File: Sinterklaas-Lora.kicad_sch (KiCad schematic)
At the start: 1 part, among them U1 Pico

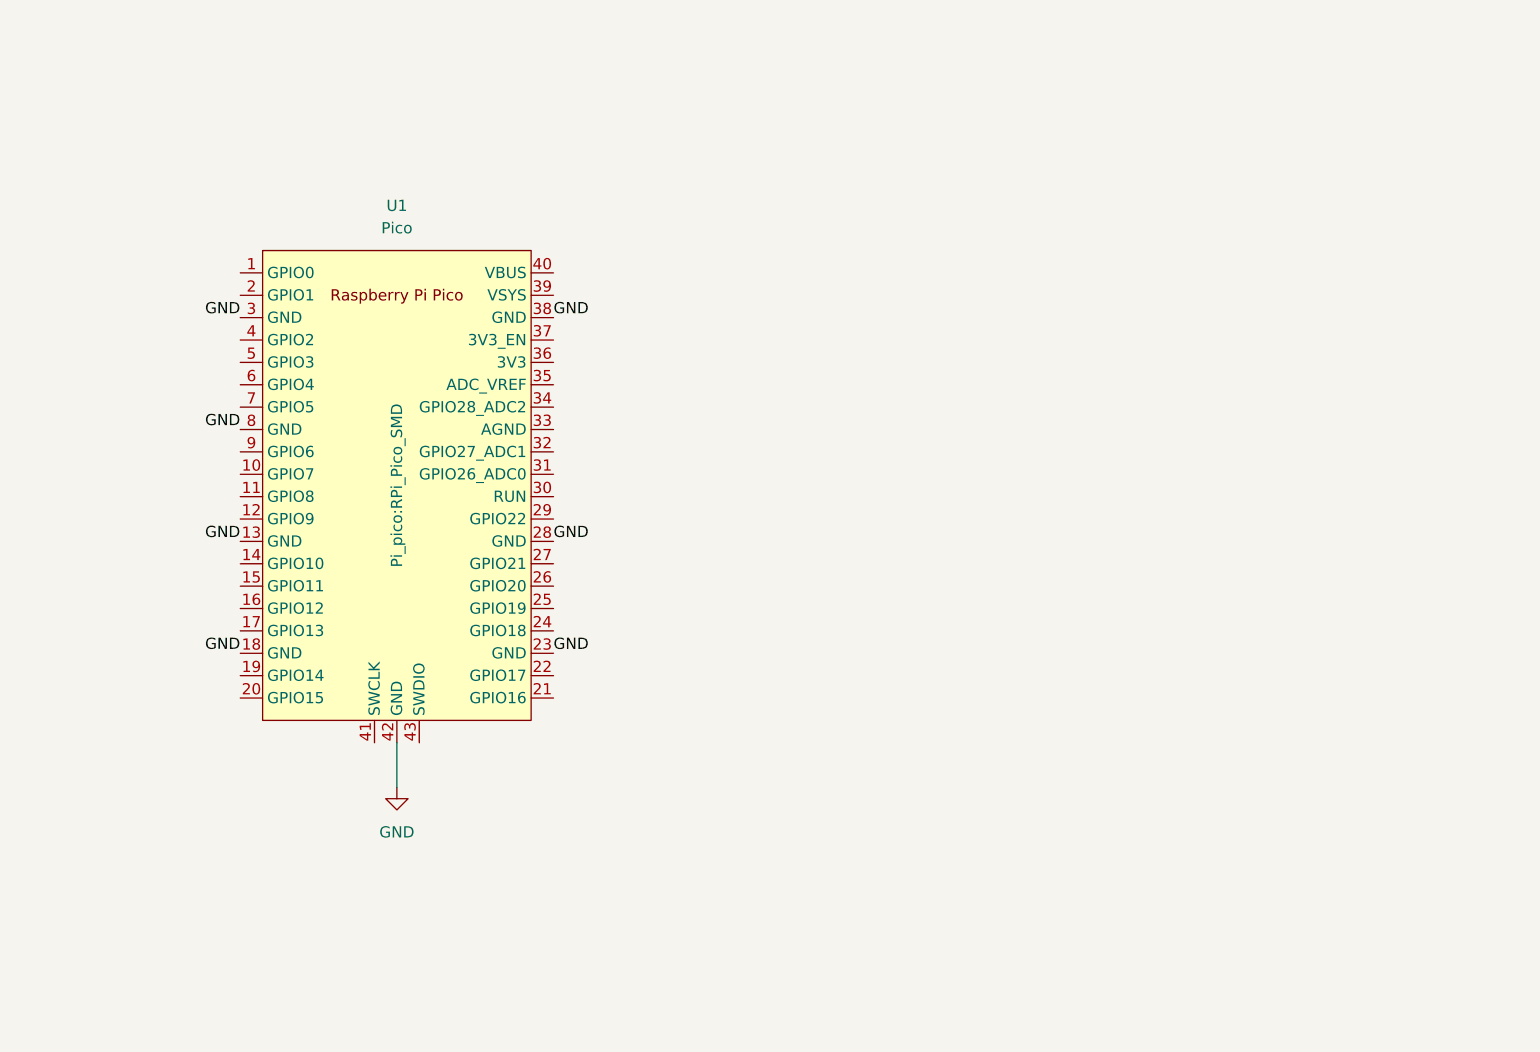
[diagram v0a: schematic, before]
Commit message: Added battery holder
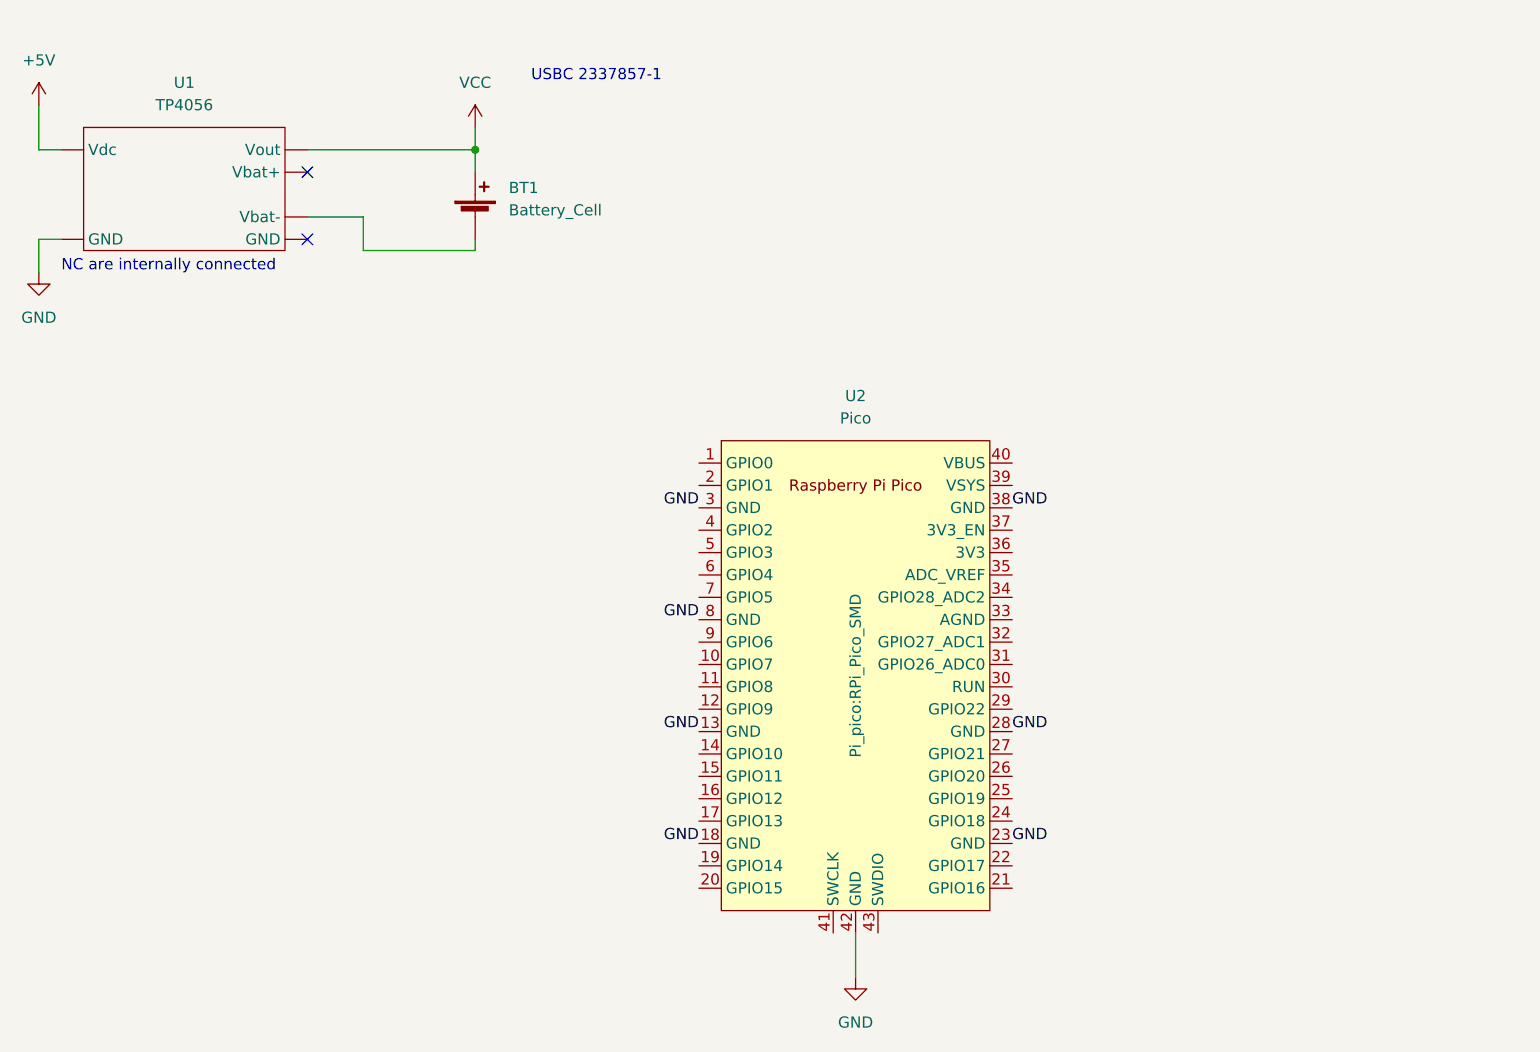
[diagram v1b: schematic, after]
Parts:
- added BT1: Battery_Cell, Pi_pico:1042P, symbol Device:Battery_Cell
- added U1: TP4056, Pi_pico:TP4056-Module, symbol _projectsymbol:TP4056
- renumbered U1 to U2
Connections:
- net GND: now also U1.2 (GND)
- new net: BT1.2 (-), U1.6 (Vbat-)
- new net +5V: U1.1 (Vdc)
- new net VCC: BT1.1 (+), U1.3 (Vout)
- no-connect marks 0 -> 2
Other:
- note added: "NC are internally connected"
- note added: "USBC 2337857-1"
- moved on the sheet: U2
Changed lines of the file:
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@@
 (kicad_sch (version 20211123) (generator eeschema)
   (paper "A3")
-  (wire (pts (xy 83.82 96.52) (xy 83.82 101.6))
-    (stroke (width 0) (type default) (color 0 0 0 0))
-  )
-  (label "GND" (at 101.6 86.36 0)
-    (effects (font (size 1.27 1.27)) (justify left bottom))
-  )
-  (label "GND" (at 66.04 60.96 180)
-    (effects (font (size 1.27 1.27)) (justify right bottom))
-  )
-  (label "GND" (at 101.6 48.26 0)
-    (effects (font (size 1.27 1.27)) (justify left bottom))
-  )
-  (label "GND" (at 66.04 48.26 180)
-    (effects (font (size 1.27 1.27)) (justify right bottom))
-  )
-  (label "GND" (at 101.6 73.66 0)
-    (effects (font (size 1.27 1.27)) (justify left bottom))
-  )
-  (label "GND" (at 66.04 73.66 180)
-    (effects (font (size 1.27 1.27)) (justify right bottom))
-  )
-  (label "GND" (at 66.04 86.36 180)
-    (effects (font (size 1.27 1.27)) (justify right bottom))
-  )
-  (symbol (lib_id "power:GND") (at 83.82 101.6 0) (unit 1)
-    (in_bom yes) (on_board yes) (fields_autoplaced)
-    (property "Reference" "#PWR0101" (id 0) (at 83.82 107.95 0)
-      (effects (font (size 1.27 1.27)) hide)
-    )
-    (property "Value" "GND" (id 1) (at 83.82 106.68 0))
-    (property "Footprint" "" (id 2) (at 83.82 101.6 0)
-      (effects (font (size 1.27 1.27)) hide)
-    )
-    (property "Datasheet" "" (id 3) (at 83.82 101.6 0)
-      (effects (font (size 1.27 1.27)) hide)
-    )
-    (pin "1")
-  )
-  (symbol (lib_id "Pi-Pico:Pico") (at 83.82 67.31 0) (unit 1)
-    (in_bom yes) (on_board yes) (fields_autoplaced)
-    (property "Reference" "U1" (id 0) (at 83.82 35.56 0))
-    (property "Value" "Pico" (id 1) (at 83.82 38.1 0))
-    (property "Footprint" "Pi_pico:RPi_Pico_SMD" (id 2) (at 83.82 67.31 90))
-    (property "Datasheet" "" (id 3) (at 83.82 67.31 0)
+  (junction (at 92.71 29.21) (diameter 0) (color 0 0 0 0)
+  )
+  (no_connect (at 73.66 39.37))
+  (no_connect (at 73.66 31.75))
+  (wire (pts (xy 73.66 36.83) (xy 80.01 36.83))
+    (stroke (width 0) (type default) (color 0 0 0 0))
+  )
+  (wire (pts (xy 92.71 26.67) (xy 92.71 29.21))
+    (stroke (width 0) (type default) (color 0 0 0 0))
+  )
+  (wire (pts (xy 43.18 43.18) (xy 43.18 39.37))
+    (stroke (width 0) (type default) (color 0 0 0 0))
+  )
+  (wire (pts (xy 43.18 29.21) (xy 45.72 29.21))
+    (stroke (width 0) (type default) (color 0 0 0 0))
+  )
+  (wire (pts (xy 73.66 29.21) (xy 92.71 29.21))
+    (stroke (width 0) (type default) (color 0 0 0 0))
+  )
+  (wire (pts (xy 43.18 39.37) (xy 45.72 39.37))
+    (stroke (width 0) (type default) (color 0 0 0 0))
+  )
+  (wire (pts (xy 43.18 24.13) (xy 43.18 29.21))
+    (stroke (width 0) (type default) (color 0 0 0 0))
+  )
+  (wire (pts (xy 92.71 29.21) (xy 92.71 31.75))
+    (stroke (width 0) (type default) (color 0 0 0 0))
+  )
+  (wire (pts (xy 135.89 118.11) (xy 135.89 123.19))
+    (stroke (width 0) (type default) (color 0 0 0 0))
+  )
+  (wire (pts (xy 80.01 40.64) (xy 92.71 40.64))
+    (stroke (width 0) (type default) (color 0 0 0 0))
+  )
+  (wire (pts (xy 80.01 36.83) (xy 80.01 40.64))
+    (stroke (width 0) (type default) (color 0 0 0 0))
+  )
+  (wire (pts (xy 92.71 40.64) (xy 92.71 39.37))
+    (stroke (width 0) (type default) (color 0 0 0 0))
+  )
+  (text "USBC 2337857-1" (at 99.06 21.59 0)
+    (effects (font (size 1.27 1.27)) (justify left bottom))
+  )
+  (text "NC are internally connected" (at 45.72 43.18 0)
+    (effects (font (size 1.27 1.27)) (justify left bottom))
+  )
+  (label "GND" (at 153.67 107.95 0)
+    (effects (font (size 1.27 1.27)) (justify left bottom))
+  )
+  (label "GND" (at 118.11 82.55 180)
+    (effects (font (size 1.27 1.27)) (justify right bottom))
+  )
+  (label "GND" (at 153.67 69.85 0)
+    (effects (font (size 1.27 1.27)) (justify left bottom))
+  )
+  (label "GND" (at 118.11 69.85 180)
+    (effects (font (size 1.27 1.27)) (justify right bottom))
+  )
+  (label "GND" (at 153.67 95.25 0)
+    (effects (font (size 1.27 1.27)) (justify left bottom))
+  )
+  (label "GND" (at 118.11 95.25 180)
+    (effects (font (size 1.27 1.27)) (justify right bottom))
+  )
+  (label "GND" (at 118.11 107.95 180)
+    (effects (font (size 1.27 1.27)) (justify right bottom))
+  )
+  (symbol (lib_id "power:GND") (at 135.89 123.19 0) (unit 1)
+    (in_bom yes) (on_board yes) (fields_autoplaced)
+    (property "Reference" "#PWR03" (id 0) (at 135.89 129.54 0)
+      (effects (font (size 1.27 1.27)) hide)
+    )
+    (property "Value" "GND" (id 1) (at 135.89 128.27 0))
+    (property "Footprint" "" (id 2) (at 135.89 123.19 0)
+      (effects (font (size 1.27 1.27)) hide)
+    )
+    (property "Datasheet" "" (id 3) (at 135.89 123.19 0)
+      (effects (font (size 1.27 1.27)) hide)
+    )
+    (pin "1")
+  )
+  (symbol (lib_id "power:VCC") (at 92.71 26.67 0) (unit 1)
+    (in_bom yes) (on_board yes) (fields_autoplaced)
+    (property "Reference" "#PWR?" (id 0) (at 92.71 30.48 0)
+      (effects (font (size 1.27 1.27)) hide)
+    )
+    (property "Value" "VCC" (id 1) (at 92.71 21.59 0))
+    (property "Footprint" "" (id 2) (at 92.71 26.67 0)
+      (effects (font (size 1.27 1.27)) hide)
+    )
+    (property "Datasheet" "" (id 3) (at 92.71 26.67 0)
+      (effects (font (size 1.27 1.27)) hide)
+    )
+    (pin "1")
+  )
+  (symbol (lib_id "Device:Battery_Cell") (at 92.71 36.83 0) (unit 1)
+    (in_bom yes) (on_board yes) (fields_autoplaced)
+    (property "Reference" "BT1" (id 0) (at 96.52 33.5279 0)
+      (effects (font (size 1.27 1.27)) (justify left))
+    )
+    (property "Value" "Battery_Cell" (id 1) (at 96.52 36.0679 0)
+      (effects (font (size 1.27 1.27)) (justify left))
+    )
+    (property "Footprint" "Pi_pico:1042P" (id 2) (at 92.71 35.306 90)
+      (effects (font (size 1.27 1.27)) hide)
+    )
+    (property "Datasheet" "~" (id 3) (at 92.71 35.306 90)
+      (effects (font (size 1.27 1.27)) hide)
+    )
+    (pin "1")
+    (pin "2")
+  )
+  (symbol (lib_id "Pi-Pico:Pico") (at 135.89 88.9 0) (unit 1)
+    (in_bom yes) (on_board yes) (fields_autoplaced)
+    (property "Reference" "U2" (id 0) (at 135.89 57.15 0))
+    (property "Value" "Pico" (id 1) (at 135.89 59.69 0))
+    (property "Footprint" "Pi_pico:RPi_Pico_SMD" (id 2) (at 135.89 88.9 90))
+    (property "Datasheet" "" (id 3) (at 135.89 88.9 0)
       (effects (font (size 1.27 1.27)) hide)
     )
@@
     (pin "9")
   )
+  (symbol (lib_id "power:GND") (at 43.18 43.18 0) (unit 1)
+    (in_bom yes) (on_board yes) (fields_autoplaced)
+    (property "Reference" "#PWR02" (id 0) (at 43.18 49.53 0)
+      (effects (font (size 1.27 1.27)) hide)
+    )
+    (property "Value" "GND" (id 1) (at 43.18 48.26 0))
+    (property "Footprint" "" (id 2) (at 43.18 43.18 0)
+      (effects (font (size 1.27 1.27)) hide)
+    )
+    (property "Datasheet" "" (id 3) (at 43.18 43.18 0)
+      (effects (font (size 1.27 1.27)) hide)
+    )
+    (pin "1")
+  )
+  (symbol (lib_id "power:+5V") (at 43.18 24.13 0) (unit 1)
+    (in_bom yes) (on_board yes) (fields_autoplaced)
+    (property "Reference" "#PWR01" (id 0) (at 43.18 27.94 0)
+      (effects (font (size 1.27 1.27)) hide)
+    )
+    (property "Value" "+5V" (id 1) (at 43.18 19.05 0))
+    (property "Footprint" "" (id 2) (at 43.18 24.13 0)
+      (effects (font (size 1.27 1.27)) hide)
+    )
+    (property "Datasheet" "" (id 3) (at 43.18 24.13 0)
+      (effects (font (size 1.27 1.27)) hide)
+    )
+    (pin "1")
+  )
+  (symbol (lib_id "_projectsymbol:TP4056") (at 59.69 33.02 0) (unit 1)
+    (in_bom yes) (on_board yes) (fields_autoplaced)
+    (property "Reference" "U1" (id 0) (at 59.69 21.59 0))
+    (property "Value" "TP4056" (id 1) (at 59.69 24.13 0))
+    (property "Footprint" "Pi_pico:TP4056-Module" (id 2) (at 59.69 25.4 0)
+      (effects (font (size 1.27 1.27)) hide)
+    )
+    (property "Datasheet" "" (id 3) (at 59.69 33.02 0)
+      (effects (font (size 1.27 1.27)) hide)
+    )
+    (pin "1")
+    (pin "2")
+    (pin "3")
+    (pin "4")
+    (pin "5")
+    (pin "6")
+  )
   (sheet_instances
     (path "/" (page "1"))
   )
   (symbol_instances
+    (path "/e896e791-75b7-4302-8882-3f5558f1f153"
+      (reference "#PWR01") (unit 1) (value "+5V") (footprint "")
+    )
+    (path "/d803e8b5-27e8-4c7f-a294-ef9de330a8a9"
+      (reference "#PWR02") (unit 1) (value "GND") (footprint "")
+    )
     (path "/324c984b-bfa5-4429-9e1d-14a5027685ce"
-      (reference "#PWR0101") (unit 1) (value "GND") (footprint "")
+      (reference "#PWR03") (unit 1) (value "GND") (footprint "")
+    )
+    (path "/632f0274-f7f1-4fc8-a701-361a8d2b438c"
+      (reference "#PWR?") (unit 1) (value "VCC") (footprint "")
+    )
+    (path "/98ca3962-d6fc-4404-a3e4-02e8452ffe62"
+      (reference "BT1") (unit 1) (value "Battery_Cell") (footprint "Pi_pico:1042P")
+    )
+    (path "/f6dd0b5d-d2c0-4f46-87f3-0c31c84ca924"
+      (reference "U1") (unit 1) (value "TP4056") (footprint "Pi_pico:TP4056-Module")
     )
     (path "/d0ab84cf-e69c-47dd-bc61-19aea5cabad0"
-      (reference "U1") (unit 1) (value "Pico") (footprint "Pi_pico:RPi_Pico_SMD")
-    )
-  )
+      (reference "U2") (unit 1) (value "Pico") (footprint "Pi_pico:RPi_Pico_SMD")
+    )
+  )

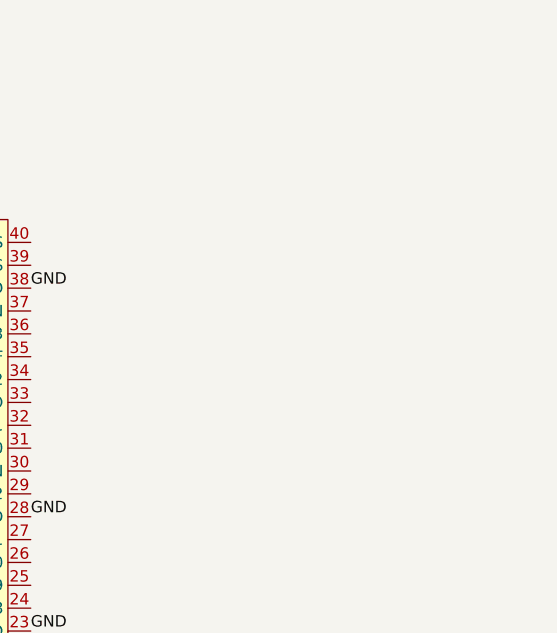
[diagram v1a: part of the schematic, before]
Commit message: Added eByte E22-900M22S module to schematic
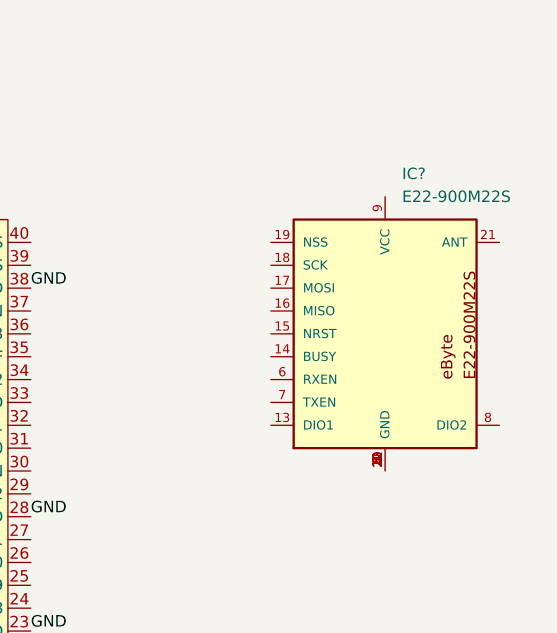
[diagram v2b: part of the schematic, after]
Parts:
- added IC?: E22-900M22S, Pi_pico:E22-900M22S, symbol _Lora:E22-900M22S
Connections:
- new net: IC?.1 (GND), IC?.10 (GND), IC?.11 (GND), IC?.12 (GND), IC?.2 (GND), IC?.20 (GND), IC?.22 (GND), IC?.3 (GND), IC?.4 (GND), IC?.5 (GND)
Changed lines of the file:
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@@
     (effects (font (size 1.27 1.27)) (justify right bottom))
+  )
+  (symbol (lib_id "_Lora:E22-900M22S") (at 193.04 74.93 0) (unit 1)
+    (in_bom yes) (on_board yes) (fields_autoplaced)
+    (property "Reference" "IC?" (id 0) (at 194.9197 57.15 0)
+      (effects (font (size 1.27 1.27)) (justify left))
+    )
+    (property "Value" "E22-900M22S" (id 1) (at 194.9197 59.69 0)
+      (effects (font (size 1.27 1.27)) (justify left))
+    )
+    (property "Footprint" "Pi_pico:E22-900M22S" (id 2) (at 193.04 74.93 0)
+      (effects (font (size 1.27 1.27)) (justify left bottom) hide)
+    )
+    (property "Datasheet" "" (id 3) (at 193.04 74.93 0)
+      (effects (font (size 1.27 1.27)) (justify left bottom) hide)
+    )
+    (pin "1")
+    (pin "10")
+    (pin "11")
+    (pin "12")
+    (pin "13")
+    (pin "14")
+    (pin "15")
+    (pin "16")
+    (pin "17")
+    (pin "18")
+    (pin "19")
+    (pin "2")
+    (pin "20")
+    (pin "21")
+    (pin "22")
+    (pin "3")
+    (pin "4")
+    (pin "5")
+    (pin "6")
+    (pin "7")
+    (pin "8")
+    (pin "9")
   )
   (symbol (lib_id "power:GND") (at 135.89 123.19 0) (unit 1)
@@
   (symbol (lib_id "power:VCC") (at 92.71 26.67 0) (unit 1)
     (in_bom yes) (on_board yes) (fields_autoplaced)
-    (property "Reference" "#PWR?" (id 0) (at 92.71 30.48 0)
+    (property "Reference" "#PWR0101" (id 0) (at 92.71 30.48 0)
       (effects (font (size 1.27 1.27)) hide)
     )
@@
     )
     (path "/632f0274-f7f1-4fc8-a701-361a8d2b438c"
-      (reference "#PWR?") (unit 1) (value "VCC") (footprint "")
+      (reference "#PWR0101") (unit 1) (value "VCC") (footprint "")
     )
     (path "/98ca3962-d6fc-4404-a3e4-02e8452ffe62"
       (reference "BT1") (unit 1) (value "Battery_Cell") (footprint "Pi_pico:1042P")
     )
+    (path "/0072b8ee-1a97-4ece-b4b7-c2f0998af4fa"
+      (reference "IC?") (unit 1) (value "E22-900M22S") (footprint "Pi_pico:E22-900M22S")
+    )
     (path "/f6dd0b5d-d2c0-4f46-87f3-0c31c84ca924"

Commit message: Added text
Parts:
- added Q1: DMG2302U, Package_TO_SOT_SMD:SOT-23, symbol Transistor_FET:DMG2302U
- gave numbers to parts that had none: 1
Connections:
- net +5V: now also U2.40 (VBUS), Q1.1 (G)
- net GND: now also IC1.1 (GND), IC1.10 (GND), IC1.11 (GND), IC1.12 (GND), IC1.2 (GND), IC1.20 (GND), IC1.22 (GND), IC1.3 (GND), IC1.4 (GND), IC1.5 (GND)
- net at IC1.13 (DIO1): now also U2.21 (GPIO16)
- net at IC1.14 (BUSY): now also U2.22 (GPIO17)
- net at IC1.16 (MISO): now also U2.24 (GPIO18)
- net at IC1.17 (MOSI): now also U2.25 (GPIO19)
- net at IC1.18 (SCK): now also U2.27 (GPIO21)
- net at IC1.19 (NSS): now also U2.29 (GPIO22)
- net RX_{EN}: now reaches IC1.6 (RXEN)
- net RX_{EN}: now also U2.6 (GPIO4)
- net TX_{EN}: now reaches IC1.7 (TXEN)
- net TX_{EN}: now also U2.7 (GPIO5)
- net DIO2: now reaches IC1.8 (DIO2)
- net DIO2: now also U2.9 (GPIO6)
- net +3.3V: now reaches IC1.9 (VCC)
- net +3.3V: now also U2.36 (3V3)
- net ~{RST}: now reaches U2.19 (GPIO14)
- net +BATT: now reaches U2.39 (VSYS)
- net +BATT: now also Q1.3 (D)
- net VCC: no longer names the net of BT1.1 (+), U1.3 (Vout)
- net VCC: now also Q1.2 (S)
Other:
- moved on the sheet: IC1
